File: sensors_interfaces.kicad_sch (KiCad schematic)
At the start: 28 parts, among them IC601 SP3485EN-L_TR, IC602 WM8782SEDS_RV_C323842, IC603 STK8321, IC604 CS4344-CZZ, IC606 MCP9700AT-E_TT, X601 CH340G, Y601 X322512MSB4SI

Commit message: start rework of baseboard.
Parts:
- renumbered C601 to C28, C602 to C29, C603 to C30, C604 to C31, C605 to C32, C606 to C33, C607 to C34, C608 to C35, C609 to C36, C610 to C37, C611 to C38, C612 to C39, C613 to C40, IC601 to IC5, IC602 to IC6, IC604 to IC7, IC603 to IC8, IC606 to IC9, L601 to L3, R601 to R53, R602 to R54, R603 to R55, R604 to R56, R605 to R57, R606 to R58, R607 to R59, X601 to X14, Y601 to Y1

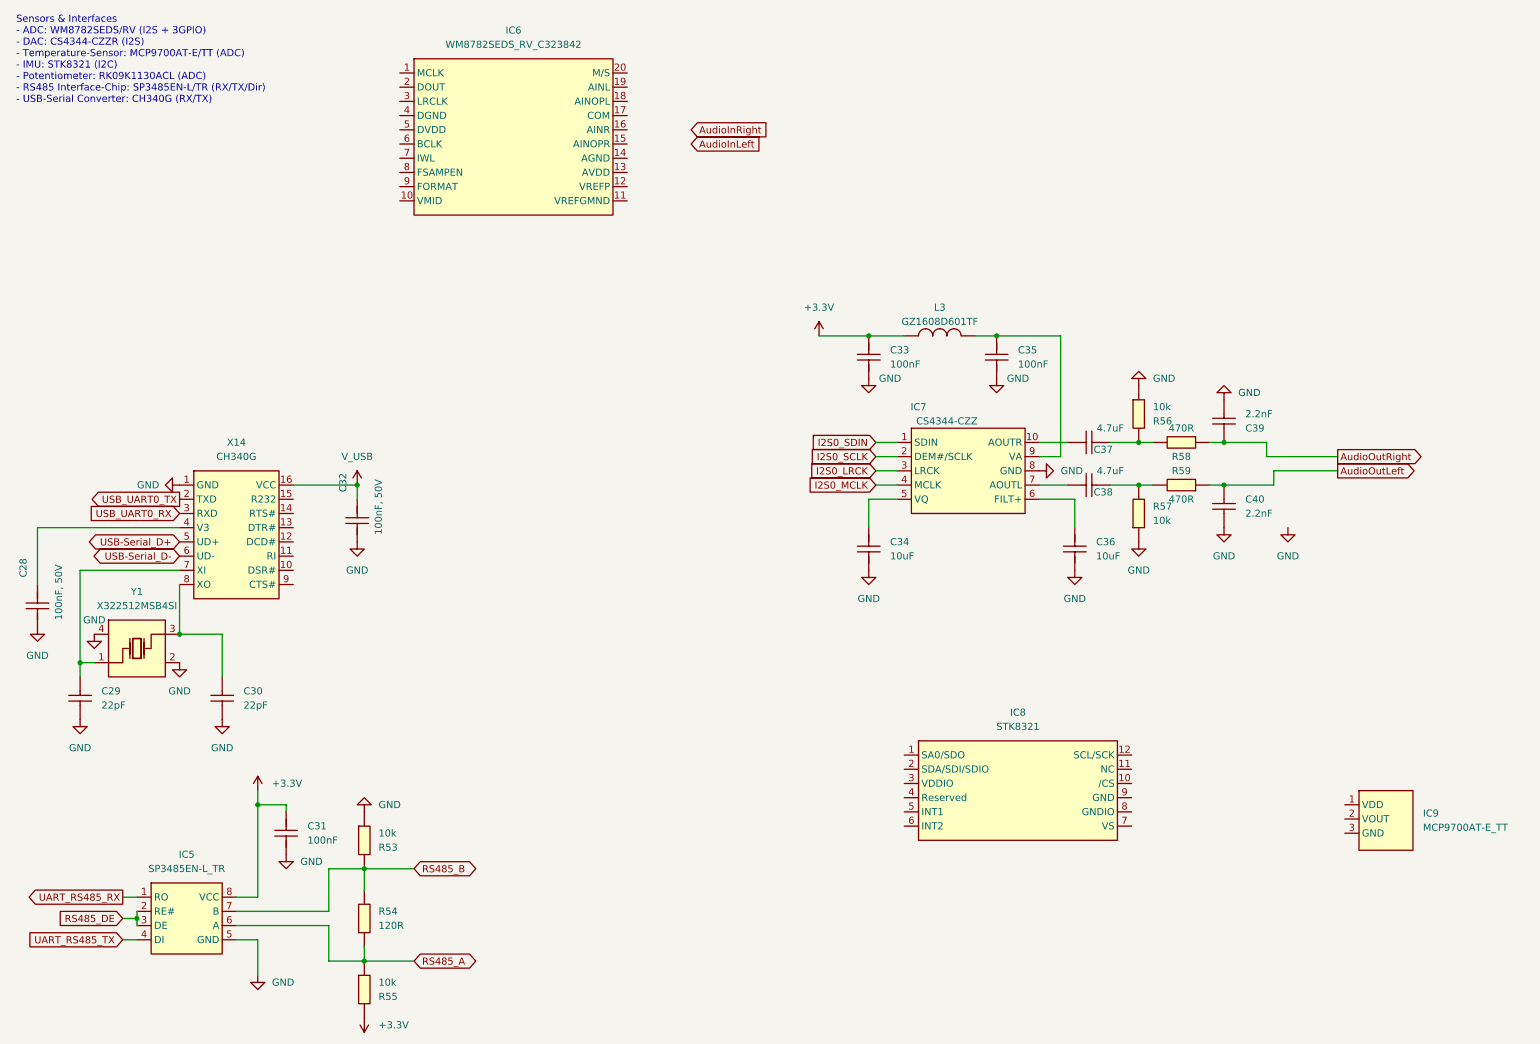
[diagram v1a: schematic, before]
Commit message: rework schematic. remove unnescessary stuff. Connect PCIE Connector. Select new Temperature Sensor (I2C) Define Signals for 40Pin Connector
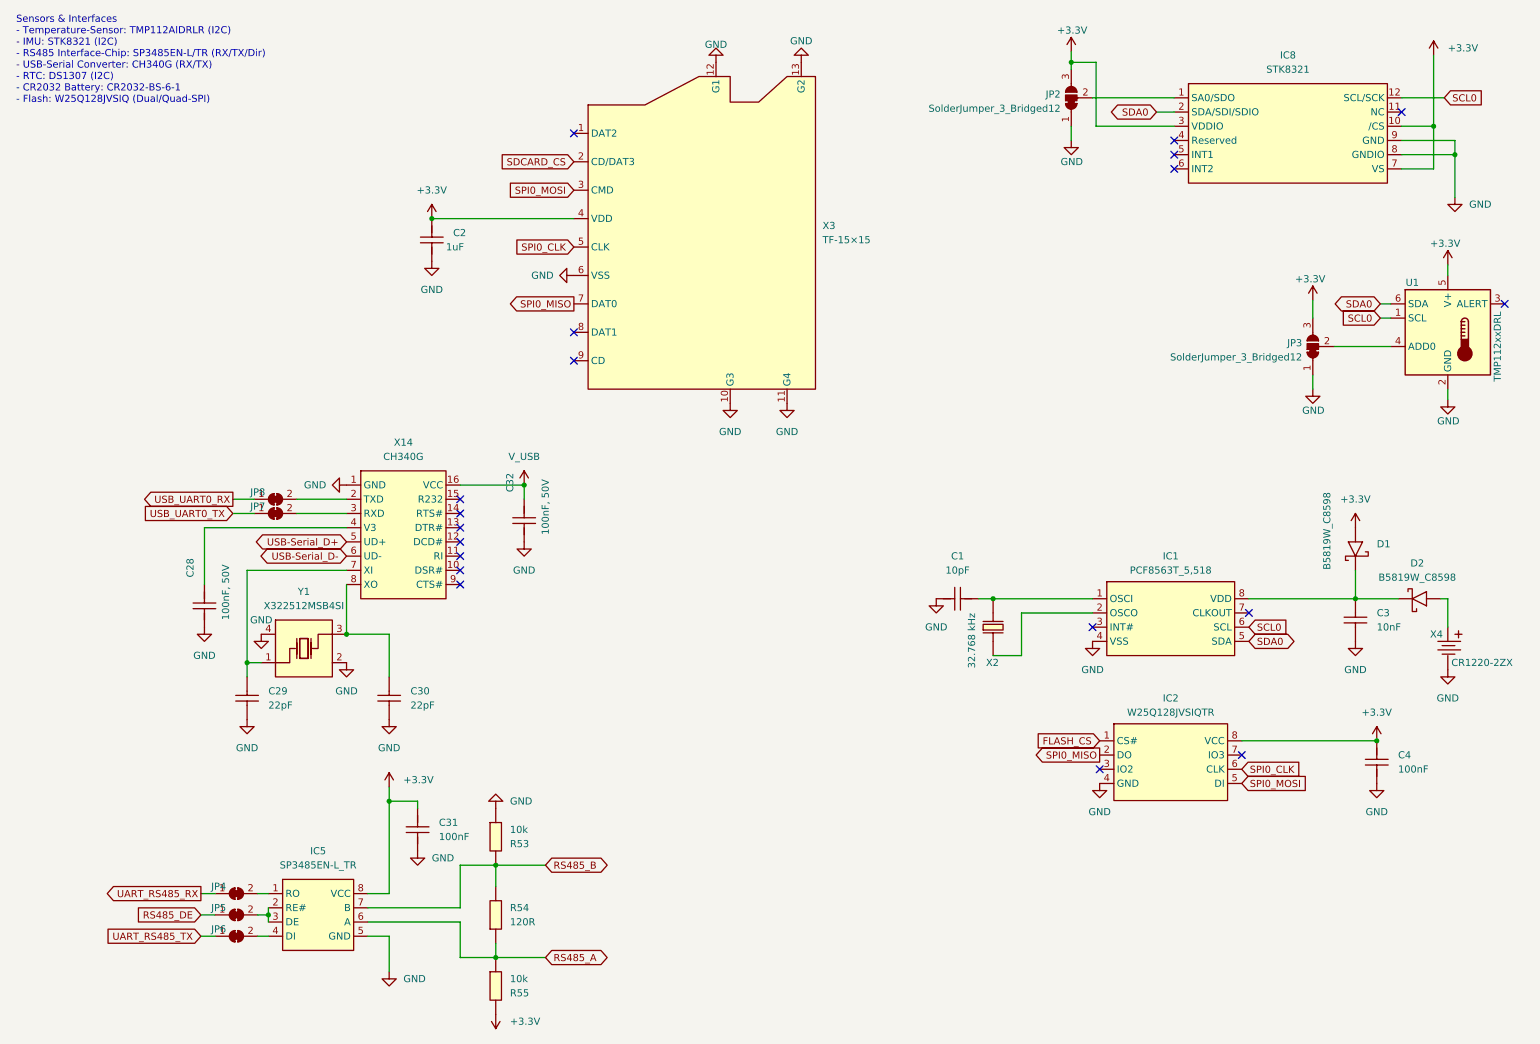
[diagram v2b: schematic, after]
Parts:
- removed C33, C35: 100nF, eduboardv2:C0402, symbol eduboardv2:CL05B104KB54PNC
- removed C34, C36: 10uF, eduboardv2:C0603, symbol eduboardv2:CL10A106MA8NRNC
- removed C37, C38: 4.7uF, eduboardv2:C0603, symbol eduboardv2:CL10A475KO8NNNC
- removed C39, C40: 2.2nF, eduboardv2:C0402, symbol eduboardv2:0402B222K500NT
- removed IC6: WM8782SEDS_RV_C323842, eduboardv2:SSOP-20_L7.5-W5.2-P0.65-LS8.0-BL, symbol eduboardv2:WM8782SEDS_RV_C323842
- removed IC7: CS4344-CZZ, eduboardv2:TSSOP-10_L3.0-W3.0-P0.50-LS4.9-BL, symbol eduboardv2:CS4344-CZZ
- removed IC9: MCP9700AT-E_TT, eduboardv2:SOT-23-3_L2.9-W1.3-P1.90-LS2.4-BR, symbol eduboardv2:MCP9700AT-E_TT
- removed L3: GZ1608D601TF, eduboardv2:L0603, symbol eduboardv2:GZ1608D601TF
- removed R56, R57: 10k, eduboardv2:R0402, symbol eduboardv2:0402WGF1002TCE
- removed R58, R59: 470R, eduboardv2:R0402, symbol eduboardv2:0402WGF4700TCE
- added C1: 10pF, eduboardv2:C0402, symbol eduboardv2:CL05C100JB5NNNC
- added C2: 1uF, eduboardv2:C0402, symbol eduboardv2:CL05A105KA5NQNC
- added C3: 10nF, eduboardv2:C0402, symbol eduboardv2:CL05B103KB5NNNC
- added C4: 100nF, eduboardv2:C0402, symbol eduboardv2:CL05B104KB54PNC
- added D1, D2: B5819W_C8598, eduboardv2:SOD-123_L2.7-W1.6-LS3.7-RD-1, symbol eduboardv2:B5819W_C8598
- added IC1: PCF8563T_5,518, eduboardv2:SOIC-8_L5.0-W4.0-P1.27-LS6.0-BL, symbol eduboardv2:PCF8563T_5,518
- added IC2: W25Q128JVSIQTR, eduboardv2:SOIC-8_L5.3-W5.3-P1.27-LS8.0-BL, symbol eduboardv2:W25Q128JVSIQTR
- added JP2, JP3: SolderJumper_3_Bridged12, symbol Jumper:SolderJumper_3_Bridged12
- added JP4, JP5, JP6, JP7, JP8: SolderJumper_2_Bridged, symbol Jumper:SolderJumper_2_Bridged
- added U1: TMP112xxDRL, Package_TO_SOT_SMD:SOT-563, symbol Sensor_Temperature:TMP112xxDRL
- added X2: 32.768 kHz, eduboardv2:FC-135R_L3.2-W1.5, symbol eduboardv2:Q13FC1350000400
- added X3: TF-15×15, eduboardv2:TF-SMD_TF-15-15, symbol eduboardv2:TF-15×15
- added X4: CR1220-2ZX, BAT-SMD_CR1220-2ZX, symbol eduboardv2:CR1220-2ZX
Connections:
- net +3.3V: now also IC8.10 (/CS), IC8.3 (VDDIO), IC8.7 (VS), C2.2, C4.2, D1.2 (+), IC2.8 (VCC), JP2.3 (B), JP3.3 (B), U1.5 (V+), X3.4 (VDD)
- net GND: now also IC8.8 (GNDIO), IC8.9 (GND), C1.2, C2.1, C3.1, C4.1, IC1.4 (VSS), IC2.4 (GND), JP2.1 (A), JP3.1 (A), U1.2 (GND), X3.10 (G3), X3.11 (G4), X3.12 (G1), X3.13 (G2), X3.6 (VSS), X4.2
- net RS485_DE: now also JP5.1 (A); no longer IC5.2 (RE#), IC5.3 (DE)
- net UART_RS485_RX: now also JP4.1 (A); no longer IC5.1 (RO)
- net UART_RS485_TX: now also JP6.1 (A); no longer IC5.4 (DI)
- net USB_UART0_RX: now also JP8.1 (A); no longer X14.3 (RXD)
- net USB_UART0_TX: now also JP7.1 (A); no longer X14.2 (TXD)
- net at IC8.1 (SA0/SDO): now also JP2.2 (C)
- net SCL0: now reaches IC8.12 (SCL/SCK)
- net SCL0: now also IC1.6 (SCL), U1.1 (SCL)
- net SDA0: now reaches IC8.2 (SDA/SDI/SDIO)
- net SDA0: now also IC1.5 (SDA), U1.6 (SDA)
- new net: IC5.1 (RO), JP4.2 (B)
- new net: IC5.2 (RE#), IC5.3 (DE), JP5.2 (B)
- new net: IC5.4 (DI), JP6.2 (B)
- new net: JP3.2 (C), U1.4 (ADD0)
- new net: C3.2, D1.1 (-), D2.1 (-), IC1.8 (VDD)
- new net: D2.2 (+), X4.1
- new net: IC1.2 (OSCO), X2.1
- new net: C1.1, IC1.1 (OSCI), X2.2
- new net: JP7.2 (B), X14.3 (RXD)
- new net: JP8.2 (B), X14.2 (TXD)
- new net FLASH_CS: IC2.1 (CS#)
- new net SDCARD_CS: X3.2 (CD/DAT3)
- new net SPI0_CLK: IC2.6 (CLK), X3.5 (CLK)
- new net SPI0_MISO: IC2.2 (DO), X3.7 (DAT0)
- new net SPI0_MOSI: IC2.5 (DI), X3.3 (CMD)
- no-connect marks 0 -> 19
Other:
- note added: "Sensors & Interfaces - Temperature-Sensor: TMP112AIDRLR (I2C) - IMU: STK8321 (I2C) - RS485 Interface-Chip: SP3485EN-L/TR (RX/TX/Dir) - USB-Serial Converter: CH340G (RX/TX) - RTC: DS1307 (I2C) - CR2032 Battery: CR2032-BS-6-1 - Flash: W25Q128JVSIQ (Dual/Quad-SPI)"
- note removed: "Sensors & Interfaces - ADC: WM8782SEDS/RV (I2S + 3GPIO) - DAC: CS4344-CZZR (I2S) - Temperature-Sensor: MCP9700AT-E/TT (ADC) - IMU: STK8321 (I2C) - Potentiometer: RK09K1130ACL (ADC) - RS485 Interface-Chip: SP3485EN-L/TR (RX/TX/Dir) - USB-Serial Converter: CH340G (RX/TX)"
- moved on the sheet: C28, C29, C30, C31, C32, IC5, IC8, R53, R54, R55, X14, Y1

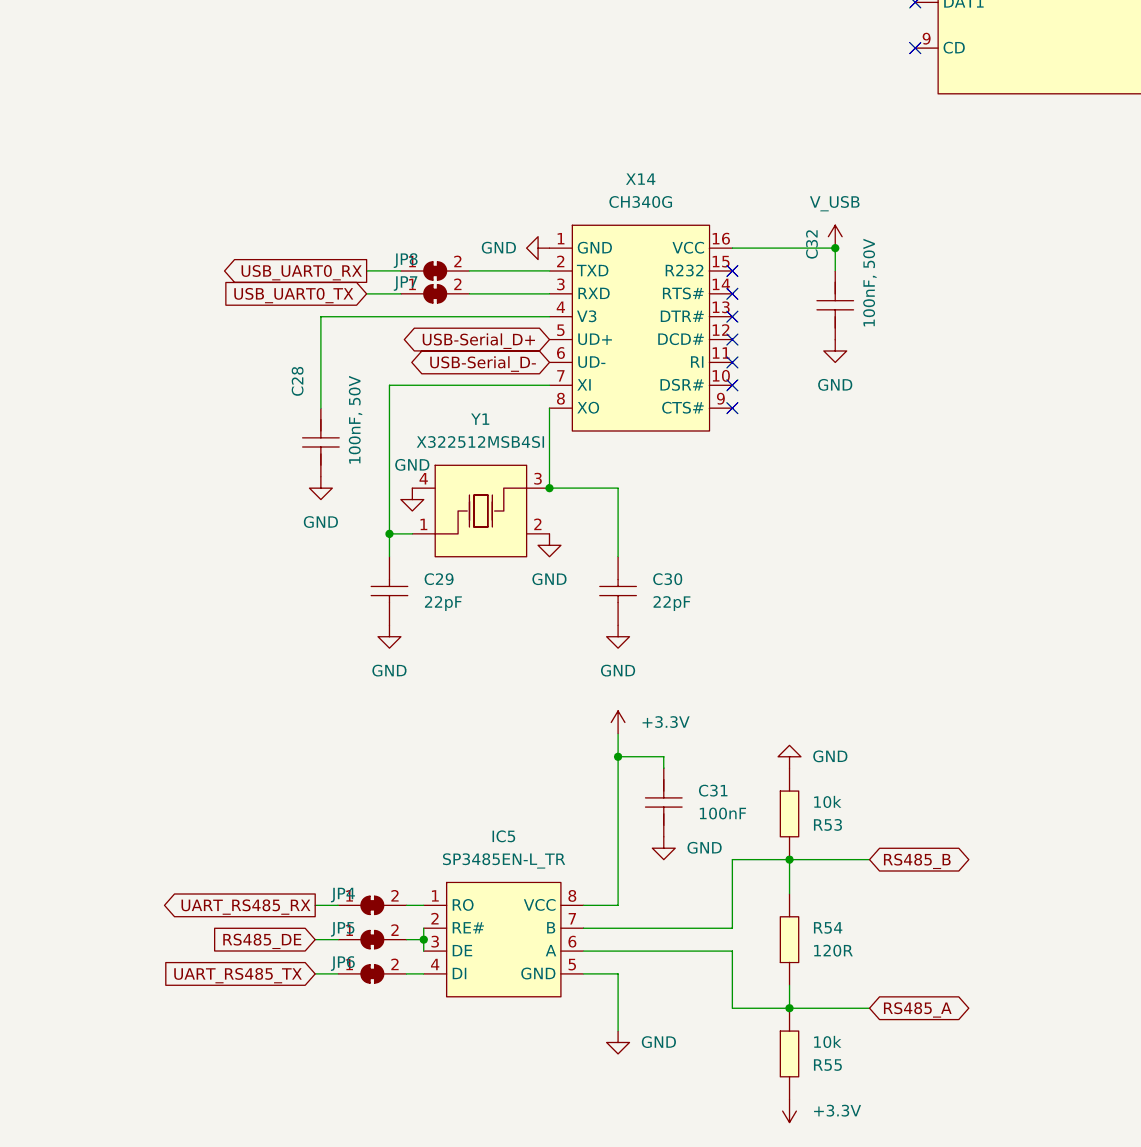
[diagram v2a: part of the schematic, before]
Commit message: replace display with better module, start layout parts on pcb.
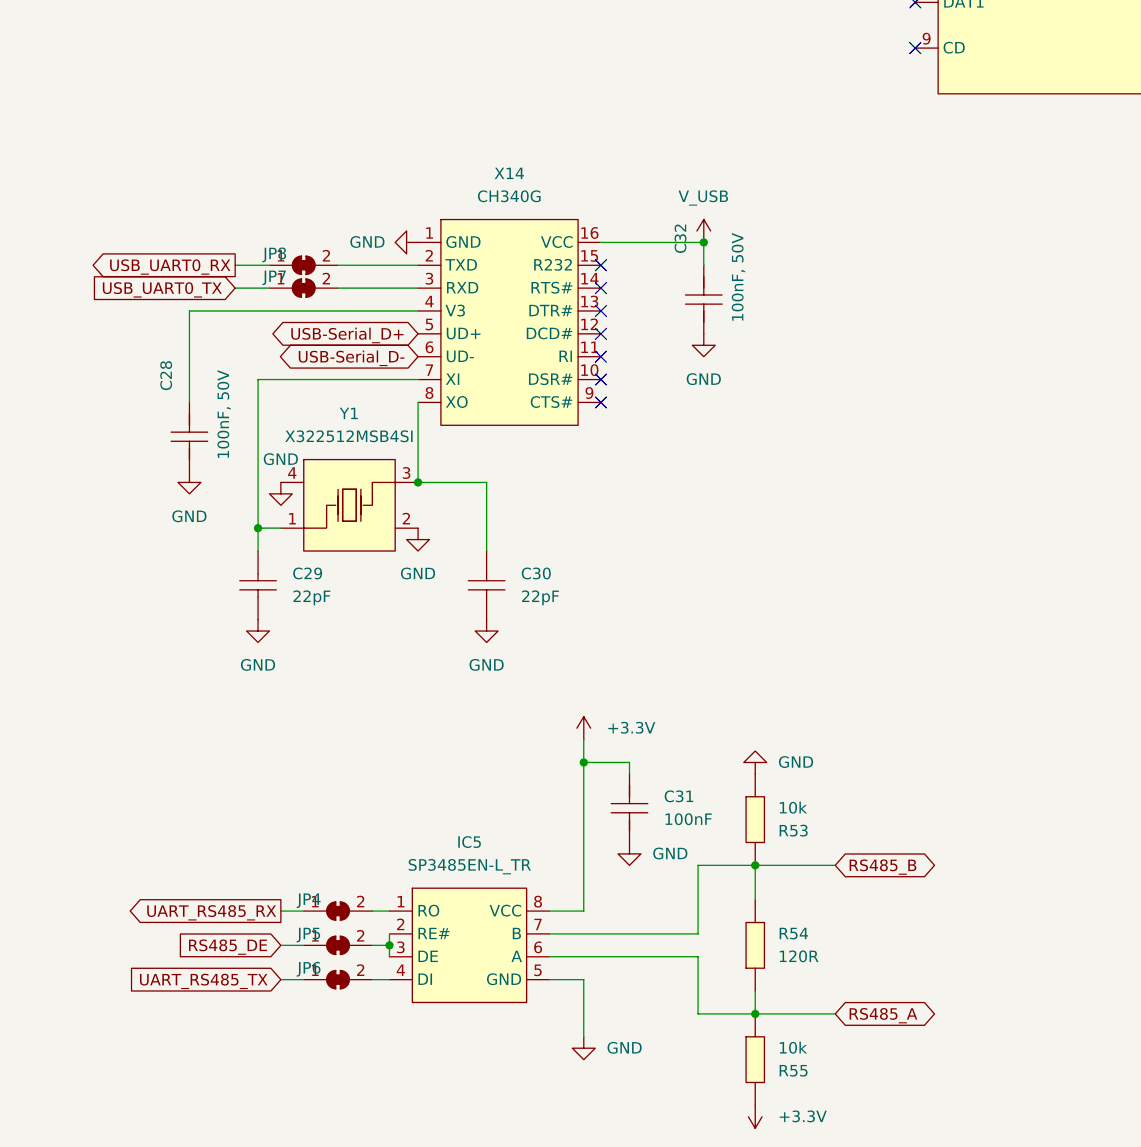
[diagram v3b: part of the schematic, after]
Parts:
- C1, C2, C28, C29, C3, C30, C31, C32, C4: footprint eduboardv2:C0402 -> Capacitor_SMD:C_0402_1005Metric_Pad0.74x0.62mm_HandSolder
- D1, D2: footprint eduboardv2:SOD-123_L2.7-W1.6-LS3.7-RD-1 -> EduboardV2_kicadlib:SOD-123_L2.7-W1.6-LS3.7-RD-1
- IC1, IC5: footprint eduboardv2:SOIC-8_L5.0-W4.0-P1.27-LS6.0-BL -> EduboardV2_kicadlib:SOIC-8_L5.0-W4.0-P1.27-LS6.0-BL
- IC2: footprint eduboardv2:SOIC-8_L5.3-W5.3-P1.27-LS8.0-BL -> EduboardV2_kicadlib:SOIC-8_L5.3-W5.3-P1.27-LS8.0-BL
- IC8: footprint eduboardv2:LGA-12_L2.0-W2.0-P0.50-TR -> EduboardV2_kicadlib:LGA-12_L2.0-W2.0-P0.50-TR
- JP2, JP3: footprint (none) -> Jumper:SolderJumper-3_P1.3mm_Bridged12_Pad1.0x1.5mm
- JP4, JP5, JP6, JP7, JP8: footprint (none) -> Jumper:SolderJumper-2_P1.3mm_Bridged_Pad1.0x1.5mm
- R53, R54, R55: footprint eduboardv2:R0402 -> Resistor_SMD:R_0402_1005Metric_Pad0.72x0.64mm_HandSolder
- X14: footprint eduboardv2:SOIC-16_L9.9-W3.9-P1.27-LS6.0-BL -> EduboardV2_kicadlib:SOIC-16_L9.9-W3.9-P1.27-LS6.0-BL
- X2: footprint eduboardv2:FC-135R_L3.2-W1.5 -> EduboardV2_kicadlib:FC-135R_L3.2-W1.5
- X3: footprint eduboardv2:TF-SMD_TF-15-15 -> EduboardV2_kicadlib:TF-SMD_TF-15-15
- X4: footprint BAT-SMD_CR1220-2ZX -> EduboardV2_kicadlib:BAT-SMD_CR1220-2ZX
- Y1: footprint eduboardv2:OSC-SMD_4P-L3.2-W2.5-BL -> EduboardV2_kicadlib:OSC-SMD_4P-L3.2-W2.5-BL
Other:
- moved on the sheet: C28, C29, C30, C31, C32, IC5, JP4, JP5, JP6, JP7, JP8, R53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

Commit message: Layout of parts done. Started laying tracks
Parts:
- added C25 (x2): 100nF, Capacitor_SMD:C_0402_1005Metric_Pad0.74x0.62mm_HandSolder, symbol eduboardv2:CL05B104KB54PNC
- added C26 (x2): 1uF, Capacitor_SMD:C_0402_1005Metric_Pad0.74x0.62mm_HandSolder, symbol eduboardv2:CL05A105KA5NQNC
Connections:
- net +3.3V: now also C25.2, C25.2, C26.2, C26.2
- net GND: now also C25.1, C25.1, C26.1, C26.1
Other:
- moved on the sheet: IC8, JP2
